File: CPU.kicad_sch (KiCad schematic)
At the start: 214 parts, among them J1 Conn_02x36_Top_Bottom, P2 Conn_02x13_Top_Bottom, P3 Conn_02x13_Top_Bottom, P4 Conn_02x08_Counter_Clockwise, P5 Conn_02x25_Counter_Clockwise, P6 Conn_02x25_Counter_Clockwise, P7 Conn_02x07_Counter_Clockwise, P8 Conn_02x08_Odd_Even

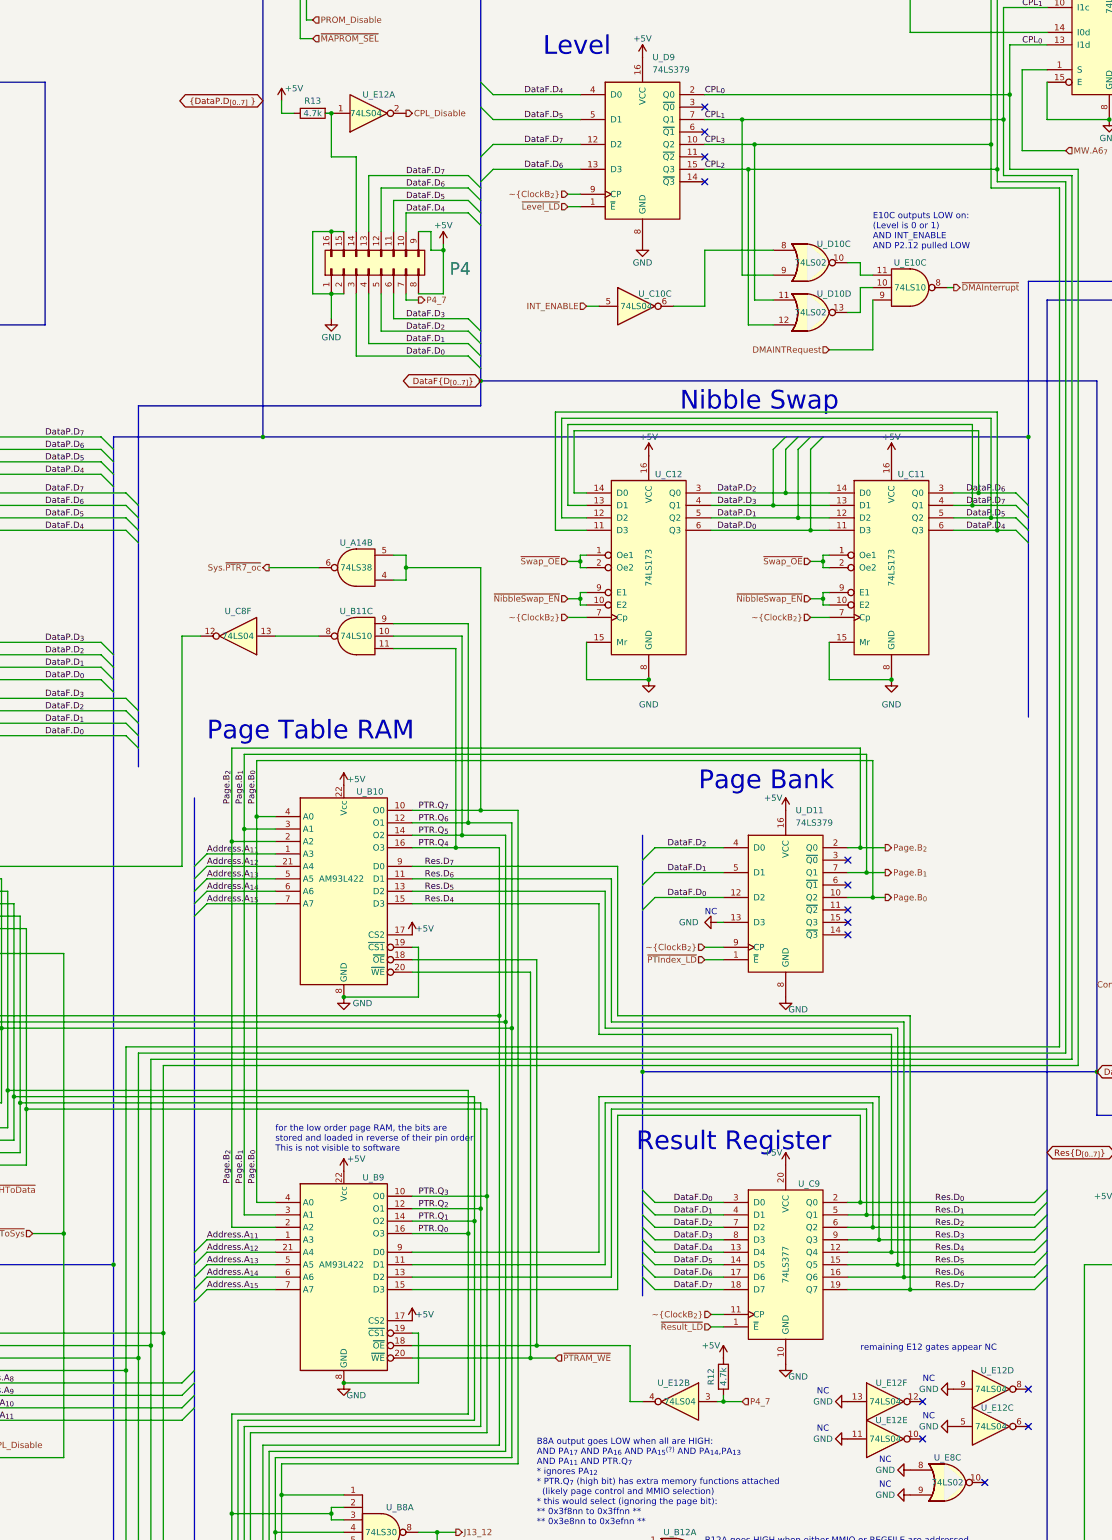
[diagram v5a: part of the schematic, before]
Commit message: P4 and U_E12 optimization
For better layout; and use IDC connector on the F bus
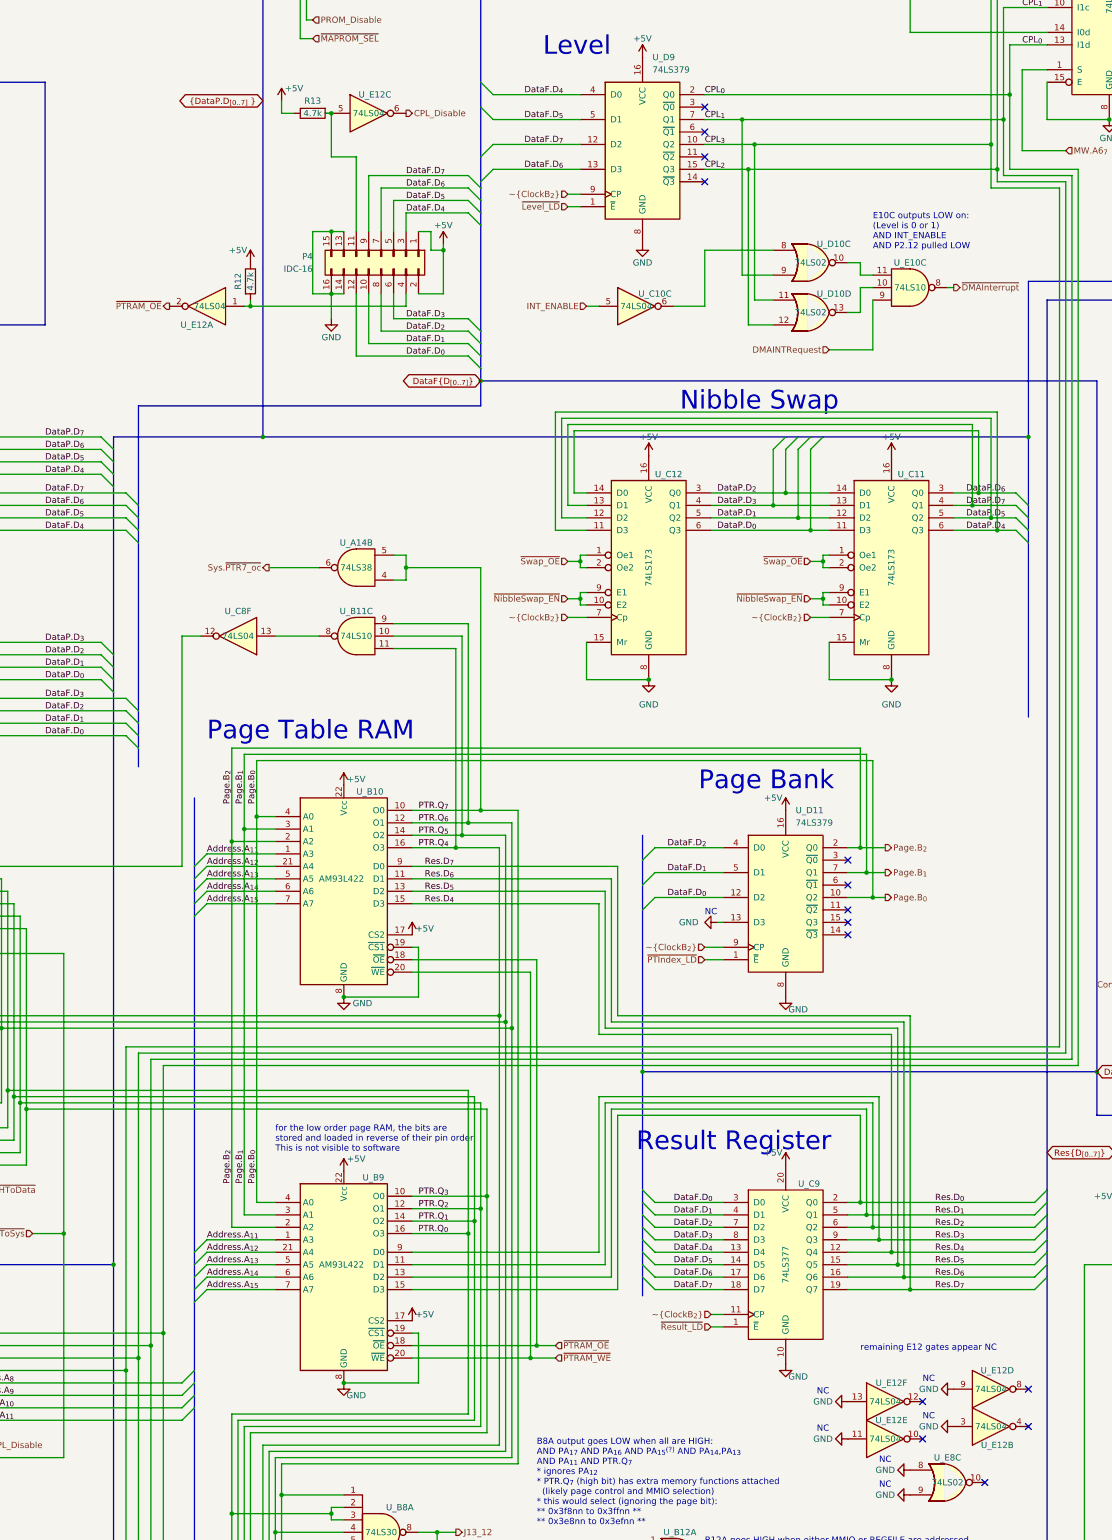
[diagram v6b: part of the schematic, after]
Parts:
- removed P4: Conn_02x08_Counter_Clockwise, Package_DIP:DIP-16_W7.62mm_Socket, symbol Connector_Generic:Conn_02x08_Counter_Clockwise
- added P4: IDC-16, Connector_IDC:IDC-Header_2x08_P2.54mm_Vertical, symbol Connector_Generic:Conn_02x08_Odd_Even
- C17, C18, C3, C8: footprint Capacitor_THT:C_Disc_D4.3mm_W1.9mm_P5.00mm -> Capacitor_THT:C_Rect_L9.0mm_W2.5mm_P7.50mm_MKT
- R17, R6: footprint Resistor_THT:R_Axial_DIN0207_L6.3mm_D2.5mm_P10.16mm_Horizontal -> Resistor_THT:R_Axial_DIN0204_L3.6mm_D1.6mm_P7.62mm_Horizontal
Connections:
- net +5V: now also P4.1 (Pin_1), P4.2 (Pin_2)
- net CPL_Disable: now also U_E12.6; no longer U_E12.2
- net DataF.D_{0}: now also P4.12 (Pin_12)
- net DataF.D_{1}: now also P4.10 (Pin_10)
- net DataF.D_{2}: now also P4.8 (Pin_8)
- net DataF.D_{3}: now also P4.6 (Pin_6)
- net DataF.D_{4}: now also P4.3 (Pin_3)
- net DataF.D_{5}: now also P4.5 (Pin_5)
- net DataF.D_{6}: now also P4.7 (Pin_7)
- net DataF.D_{7}: now also P4.9 (Pin_9)
- net GND: now also U_E12.3, P4.13 (Pin_13), P4.14 (Pin_14), P4.15 (Pin_15), P4.16 (Pin_16); no longer U_E12.5
- net at R13.2: now also U_E12.5, P4.11 (Pin_11); no longer U_E12.1
- net ~{PTRAM_OE}: now reaches U_B10.18 (~{OE}), U_B9.18 (~{OE})
- net ~{PTRAM_OE}: now also U_E12.2; no longer U_E12.4
- net P4_7: no longer names the net of R12.2
- net P4_7: now also U_E12.1, P4.4 (Pin_4); no longer U_E12.3

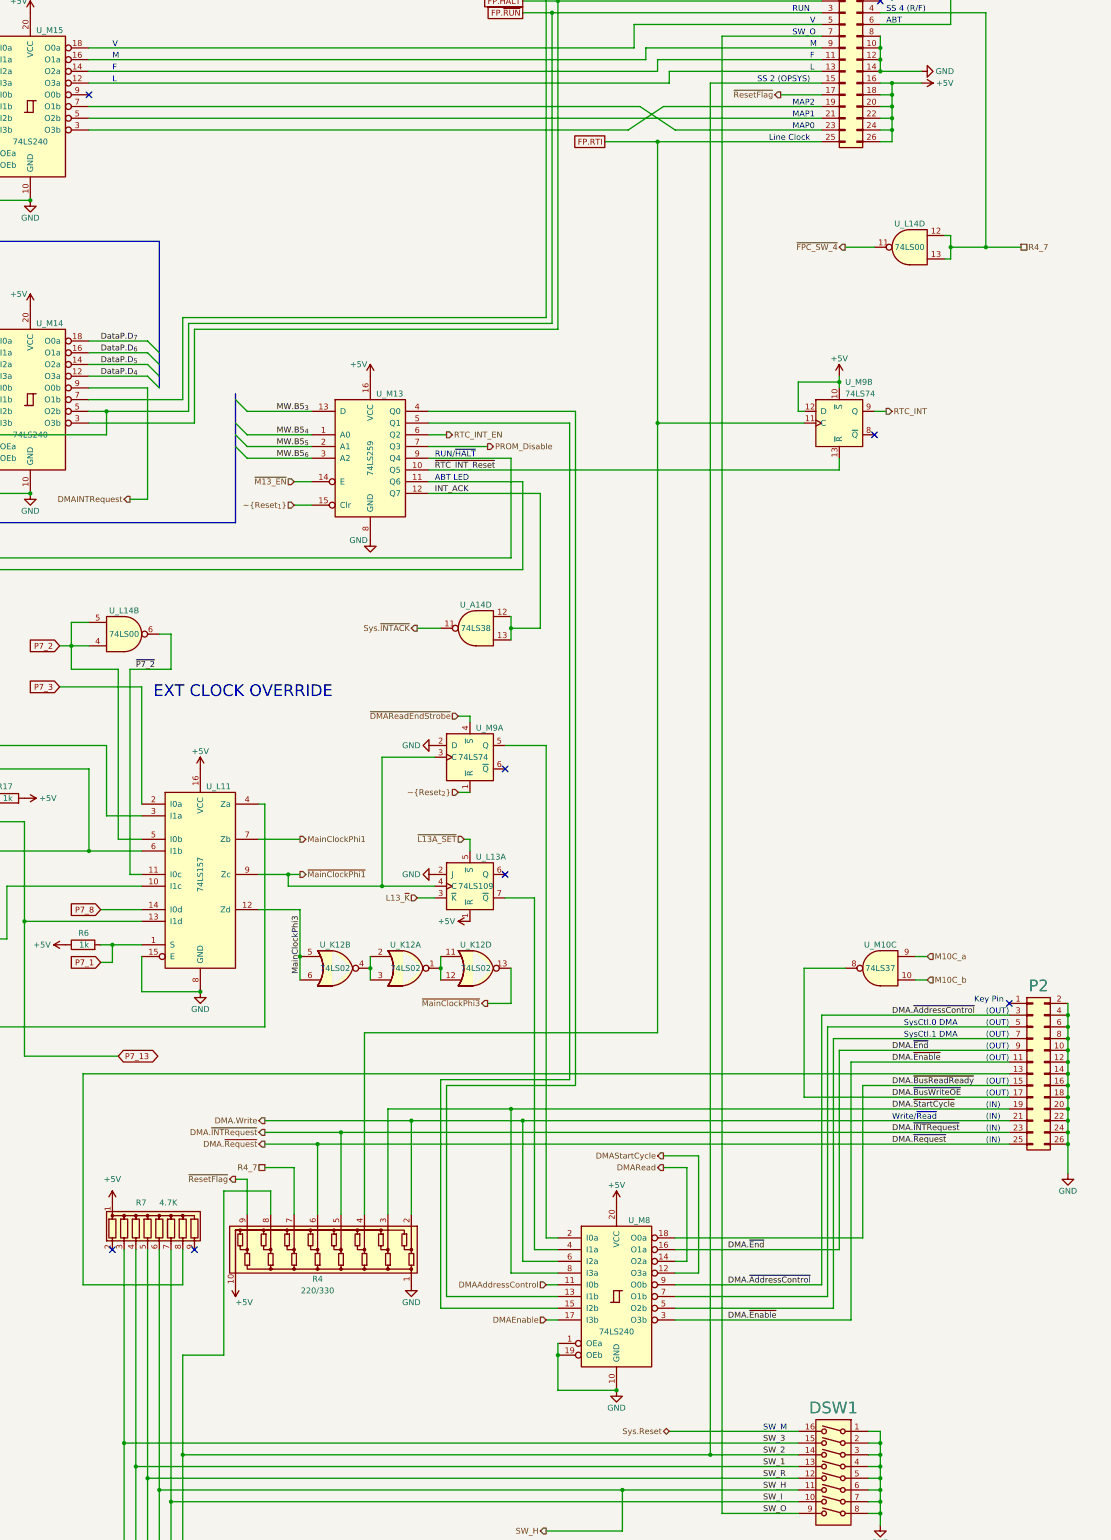
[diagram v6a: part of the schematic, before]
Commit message: Split divider network RN4
Separated into individual single-resistor components for routing optimization
and easier access
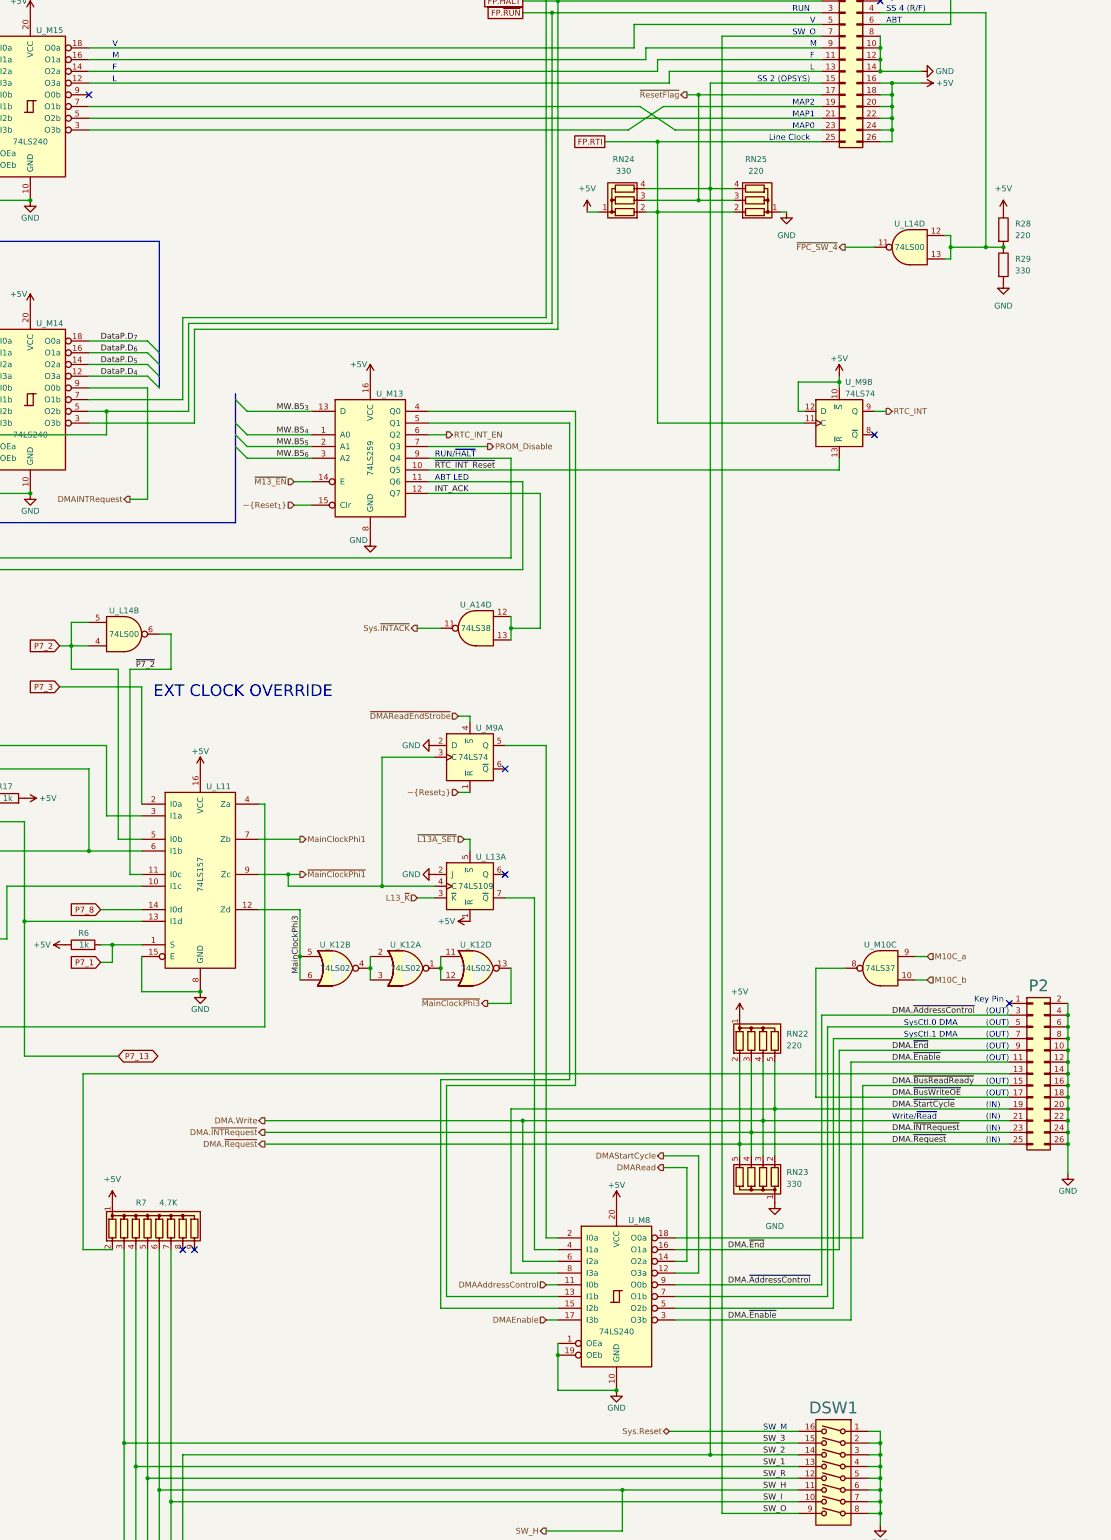
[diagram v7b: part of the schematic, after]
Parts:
- removed R4: 220/330, Resistor_THT:R_Array_SIP10, symbol Device:R_Network_Dividers_x08_SIP
- added R28: 220, Resistor_THT:R_Axial_DIN0204_L3.6mm_D1.6mm_P2.54mm_Vertical, symbol Device:R
- added R29: 330, Resistor_THT:R_Axial_DIN0204_L3.6mm_D1.6mm_P2.54mm_Vertical, symbol Device:R
- added RN22: 220, Resistor_THT:R_Array_SIP5, symbol Device:R_Network04
- added RN23: 330, Resistor_THT:R_Array_SIP5, symbol Device:R_Network04
- added RN24: 330, Resistor_THT:R_Array_SIP4, symbol Device:R_Network03
- added RN25: 220, Resistor_THT:R_Array_SIP4, symbol Device:R_Network03
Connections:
- net +5V: now also R28.1, RN22.1 (common), RN24.1 (common)
- net DMA.Write: now also RN22.4 (R3), RN23.3 (R2)
- net DMA.~{INTRequest}: now also RN22.3 (R2), RN23.4 (R3)
- net DMA.~{Request}: now also RN22.2 (R1), RN23.5 (R4)
- net DMA.~{StartCycle}: now also RN22.5 (R4), RN23.2 (R1)
- net FP.RTI: now also RN24.2 (R1), RN25.2 (R1)
- net GND: now also R29.2, RN23.1 (common), RN25.1 (common)
- net SW_2: now also RN24.4 (R3), RN25.4 (R3)
- net ~{ResetFlag}: now also RN24.3 (R2), RN25.3 (R2)
- net at R7.2 (R1): now also P2.13 (Pin_13)
- net at R7.8 (R7): no longer P2.13 (Pin_13)
- net R4_7: no longer names the net of P3.4 (Pin_4), U_L14.12, U_L14.13
- net R4_7: now also R28.2, R29.1
